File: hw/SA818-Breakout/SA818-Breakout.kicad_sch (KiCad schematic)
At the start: 32 parts, among them J1 Conn_Coaxial, J2 Conn_01x02, J3 Conn_01x10, Q1 BSS138, Q2 BSS138, Q3 BSS138, Q4 BSS138, U10 NCP1117-5.0_SOT223, U11 NCP1117-3.3_SOT223

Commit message: Updating PCB
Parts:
- removed C3: 22u, Capacitor_SMD:C_0805_2012Metric_Pad1.18x1.45mm_HandSolder, symbol Device:C_Small
- removed Q1, Q2, Q3, Q4: BSS138, Package_TO_SOT_SMD:SOT-23, symbol Transistor_FET:BSS138
- removed R1, R2, R3, R4, R5, R6, R7, R8: 10k, Resistor_SMD:R_0805_2012Metric_Pad1.20x1.40mm_HandSolder, symbol Device:R_Small_US
- removed R10: 4.7, Resistor_SMD:R_0805_2012Metric_Pad1.20x1.40mm_HandSolder, symbol Device:R_Small_US
- removed TP9: TestPoint, TestPoint:TestPoint_Pad_2.5x2.5mm, symbol Connector:TestPoint
- removed U11: NCP1117-3.3_SOT223, Package_TO_SOT_SMD:SOT-223-3_TabPin2, symbol Regulator_Linear:NCP1117-3.3_SOT223
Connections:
- net AFSQ_5 is gone; now on net AFSQ_3: C6.1, U1.1 (~{AF_SQ})
- net PTT_5 is gone; now on net PTT_3: C5.1, U1.5 (~{PTT})
- net RXD_5 is gone; now on net RXD_3: U1.16 (RXD)
- net TXD_5 is gone; now on net TXD_3: U1.17 (TXD)
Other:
- note removed: "+3.3V Source"
- note removed: "Level Shifting"

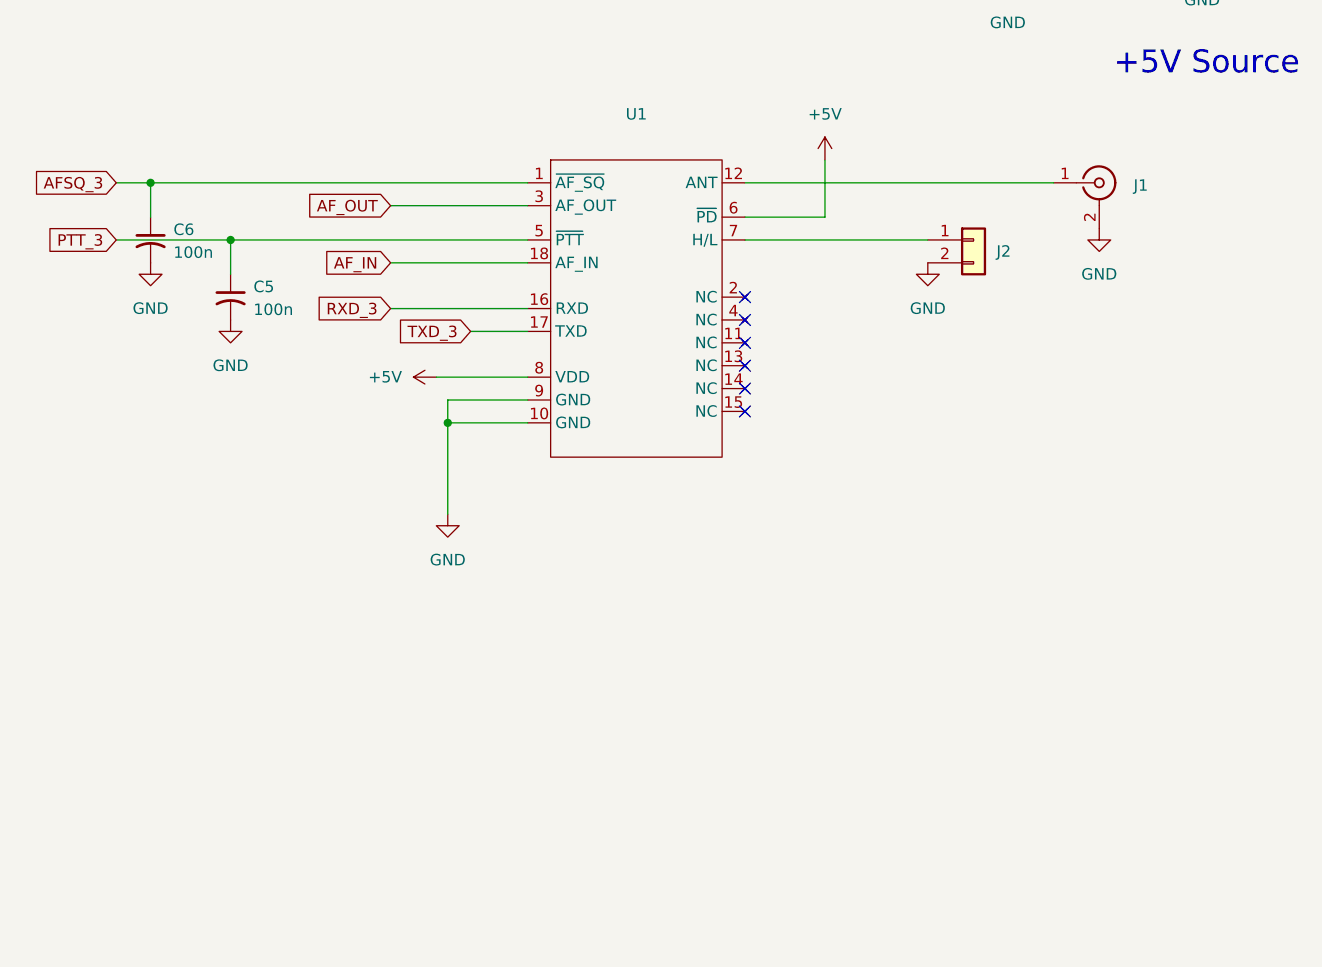
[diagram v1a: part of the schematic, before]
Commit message: Added LPF for harmonics
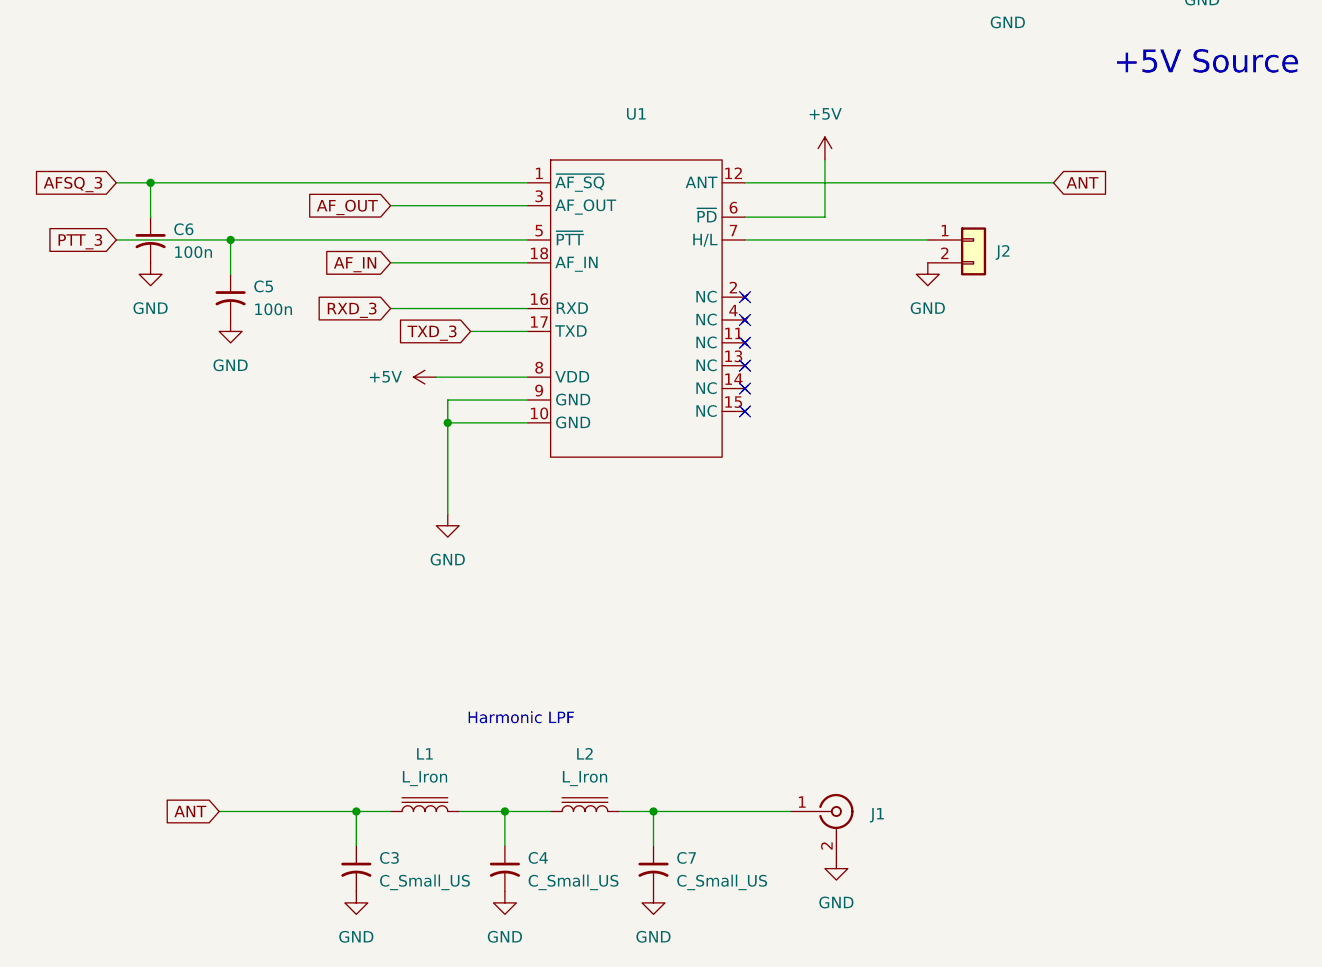
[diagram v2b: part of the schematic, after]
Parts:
- added C3, C4, C7: C_Small_US, Capacitor_SMD:C_0805_2012Metric_Pad1.18x1.45mm_HandSolder, symbol Device:C_Small_US
- added L1, L2: L_Iron, Inductor_THT:L_Axial_L6.6mm_D2.7mm_P10.16mm_Horizontal_Vishay_IM-2, symbol Device:L_Iron
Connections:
- net GND: now also C3.2, C4.2, C7.2
- net at J1.1 (In): now also C7.1, L2.2; no longer U1.12 (ANT)
- new net: C4.1, L1.2, L2.1
- new net ANT: C3.1, L1.1, U1.12 (ANT)
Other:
- note added: "Harmonic LPF"
- moved on the sheet: J1

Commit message: Updated 50ohm traces
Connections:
- net ANT_OUT: now reaches C7.1, J1.1 (In), L2.2
- net LPF1: now reaches C4.1, L1.2, L2.1
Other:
- note added: "MAKE SURE THIS IS A >+12V COMPLIANT CAP!"
- note removed: "MAKE SURE THIS IS A +12V CAP!"
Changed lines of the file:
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@@
 	(title_block
 		(title "SA818 Breakout")
-		(date "2025-10-07")
+		(date "2025-10-09")
 		(rev "1")
 		(company "Bruce MacKinnon KC1FSZ")
@@
 	(text "+5V Source"
 		(exclude_from_sim no)
-		(at 155.448 52.832 0)
+		(at 154.178 22.606 0)
 		(effects
 			(font
@@
 		)
 	)
-	(text "MAKE SURE THIS \nIS A +12V CAP!"
+	(text "MAKE SURE THIS \nIS A >+12V COMPLIANT CAP!"
 		(exclude_from_sim no)
-		(at 133.858 30.226 0)
+		(at 117.602 39.878 0)
 		(effects
 			(font
@@
 	(text "Per datasheet: \"output capacitor minimum of \n4.7uF with ESR in range of 33mO to 2.2O\"\n\nUsing series resistor."
 		(exclude_from_sim no)
-		(at 142.748 23.876 0)
+		(at 177.292 43.942 0)
 		(effects
 			(font
@@
 		)
 	)
+	(label "ANT_OUT"
+		(at 99.06 135.89 0)
+		(effects
+			(font
+				(size 1.27 1.27)
+			)
+			(justify left bottom)
+		)
+	)
+	(label "LPF1"
+		(at 73.66 135.89 0)
+		(effects
+			(font
+				(size 1.27 1.27)
+			)
+			(justify left bottom)
+		)
+	)
